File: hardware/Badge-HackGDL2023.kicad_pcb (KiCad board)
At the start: 2 copper layers, 15 parts, among them J1 SWD, SW1 SW_RST, SW2 On, U1 PY32F002AA15M6TU

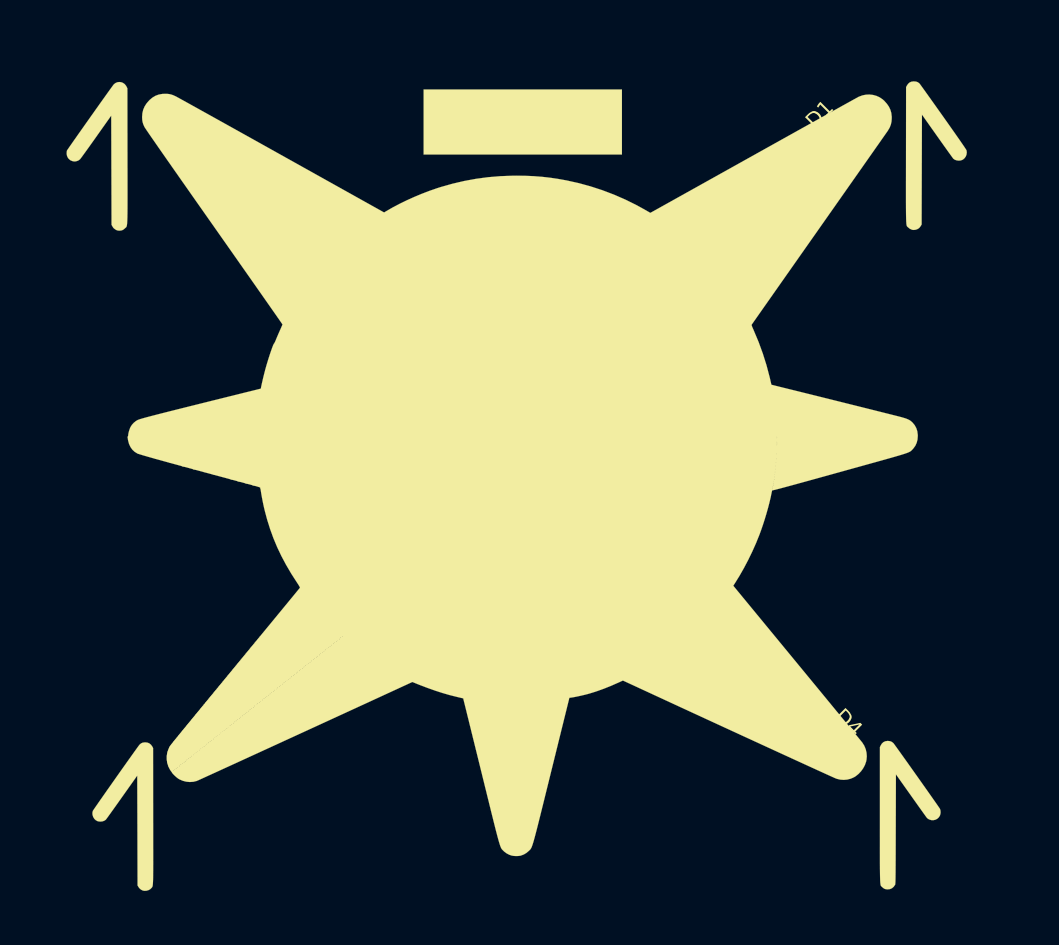
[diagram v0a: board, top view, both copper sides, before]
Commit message: add first edge cuts
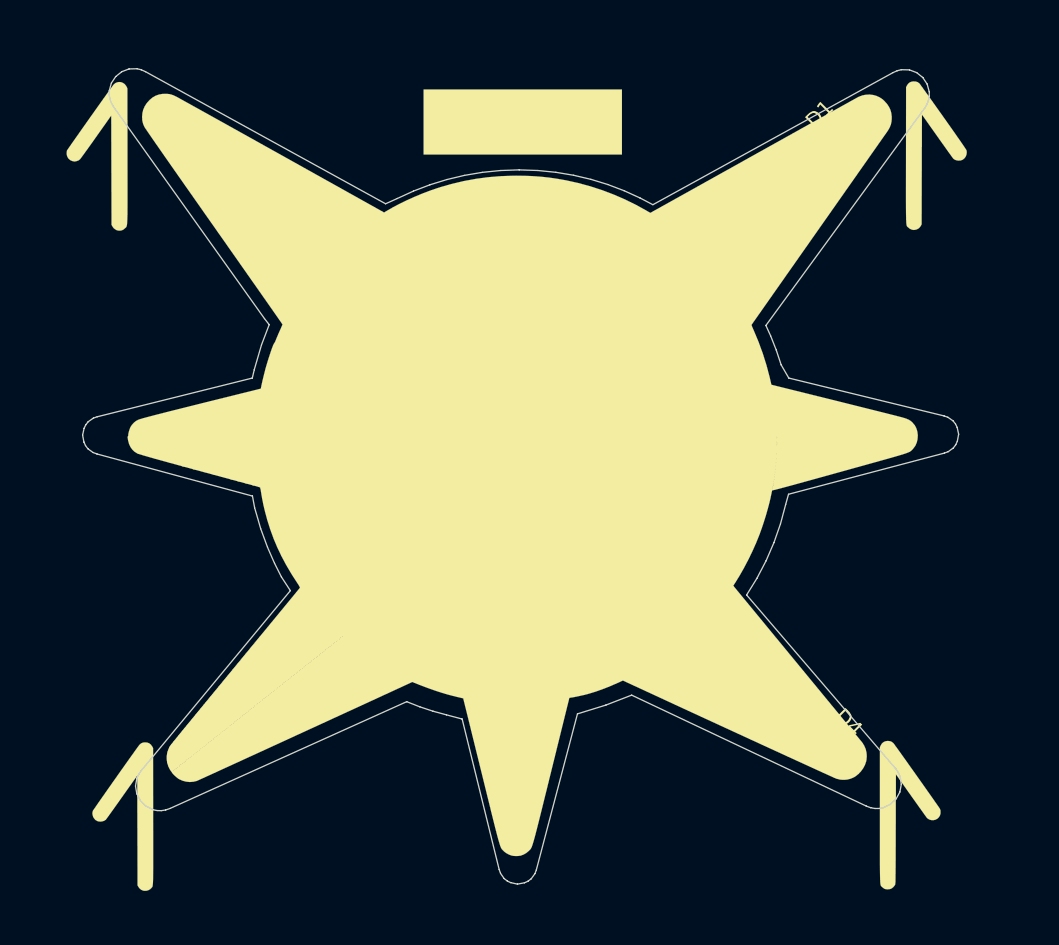
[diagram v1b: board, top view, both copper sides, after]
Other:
- board outline added: 58.4 x 54.4 mm

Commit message: Update routing
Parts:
- removed Ref**: Val**, Footprints:LOGO PRINCIPAL FONDO BLANCO
- added ?: , , F.Cu at (225.3, 63.8)
- added kibuzzard-65BC4D69: G***, kibuzzard-65BC4D69, B.Cu at (227.4, 95.0)
- added kibuzzard-65BC4D87: G***, kibuzzard-65BC4D87, B.Cu at (227.4, 92.4)
- added kibuzzard-65BC4E20: G***, kibuzzard-65BC4E20, B.Cu at (227.6, 89.8)
- moved SW2 15.5 mm to (240.3, 55.8), turned to 29 degrees
- moved R1 5.87 mm to (248.4, 52.3), turned to -135 degrees
- moved SW1 2.98 mm to (216.7, 60.6), turned to 180 degrees
- moved D1 2.01 mm to (248.4, 52.3)
- moved D2 1.79 mm to (201.9, 52.1)
- moved R2 1.66 mm to (205.4, 55.6)
- moved D3 1.38 mm to (203.9, 94.2)
- moved R4 1.17 mm to (242.3, 89.9)
- moved BT1 1.13 mm to (234.4, 74.3)
- moved R3 1.11 mm to (207.4, 90.7)
- moved D4 0.40 mm to (245.8, 93.4)
- moved J1 0.23 mm to (225.1, 89.9)
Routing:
- net +3.3V: track 0.00 -> 85.9 mm, vias 0 -> 4
- net /PA1: track 0.00 -> 49.8 mm, vias 0 -> 1
- net /PA6: track 0.00 -> 44.9 mm, vias 0 -> 1
- net /PF0: track 0.00 -> 35.4 mm, vias 0 -> 1
- net /PA7: track 0.00 -> 29.4 mm, vias 0 -> 1
- net /SWDIO: track 0.00 -> 23.7 mm
- net /SWCLK: track 0.00 -> 22.2 mm, vias 0 -> 2
- net Net-(BT1--): track 0.00 -> 20.4 mm
- net /NRST: track 0.00 -> 17.1 mm
- net Net-(D1-K): track 0.00 -> 3.36 mm, vias 0 -> 1
- net Net-(D2-K): track 0.00 -> 3.12 mm, vias 0 -> 1
- net Net-(D3-K): track 0.00 -> 3.11 mm, vias 0 -> 1
- net Net-(D4-K): track 0.00 -> 3.09 mm, vias 0 -> 1
- net GND: vias 0 -> 17
- added copper zone on B.Cu, net GND
- added copper zone on F.Cu, net GND

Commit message: update labels
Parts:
- added G***: LOGO, LOGO, F.Cu at (225.2, 77.1)
- added G***: LOGO, Aesthetics:electronic_cats_logo_8x6, B.Cu at (219.2, 83.3)
- added kibuzzard-65BD0189: G***, kibuzzard-65BD0189, B.Cu at (216.8, 64.9)
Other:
- board text added: "Broken Access Control"
- board text added: "Cryptographic Failures"
- board text added: "Injection"
- board text added: "Insecure Design"
- board text added: "Security Misconfiguration"
- board text added: "Tequila"
- board text added: "Viva el Hacking"
- board text added: "Vulnerable Components"
- board text added: "v1.0"

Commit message: update v1.0
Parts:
- moved kibuzzard-65BC4D69 2.61 mm to (227.6, 92.4)
- moved kibuzzard-65BC4D87 2.60 mm to (227.4, 95.0)
- moved ? 1.03 mm to (225.3, 62.8)
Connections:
- J1 pad 2: /SWCLK -> /SWDIO
- J1 pad 3: /SWDIO -> /SWCLK
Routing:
- net /SWCLK: track 22.2 -> 25.1 mm, vias 2 -> 0
- net /SWDIO: track 23.7 -> 21.7 mm
- net /PF0: track 35.4 -> 33.9 mm
- net /PA1: track 49.8 -> 50.5 mm
- net GND: vias 17 -> 18
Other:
- outline, holes or cut-outs redrawn
